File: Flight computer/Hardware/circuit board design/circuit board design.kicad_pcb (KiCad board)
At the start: 4 copper layers, 30.5 x 82.6 mm, 89 parts, among them J1 Conn_01x05, J2 USB_B_Micro, J3 Screw_Terminal_01x04, J4 Conn_01x02, J5 Screw_Terminal_01x04, J6 Conn_Coaxial, J7 Conn_Coaxial, U1 IIS2MDC, U10 BMI088, U11 ATSAML21J18B-AUT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

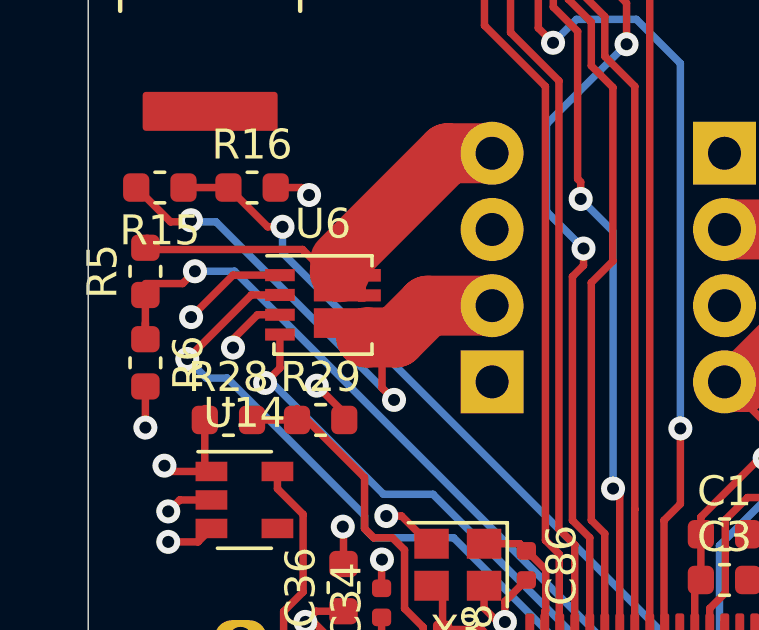
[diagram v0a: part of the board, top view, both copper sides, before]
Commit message: changed power plane to 3.3V, bringing v drive to pins via 2.54mm tracks
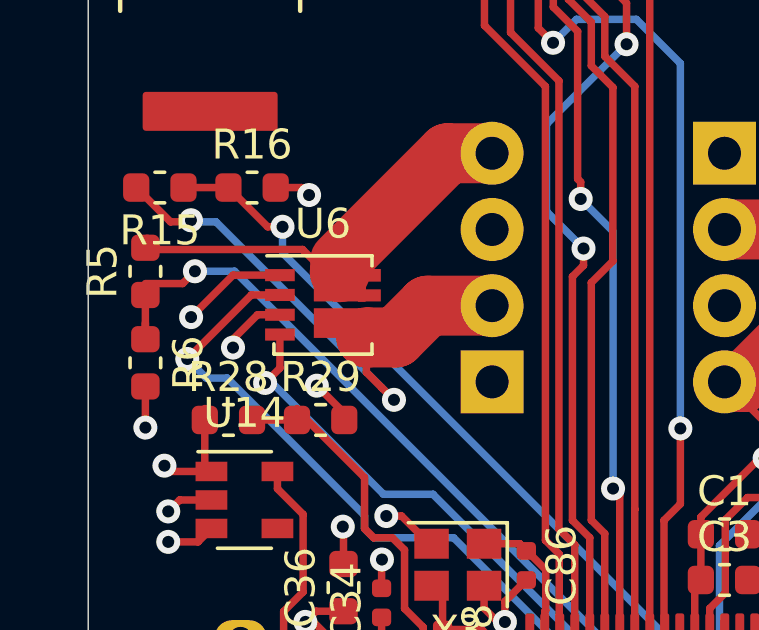
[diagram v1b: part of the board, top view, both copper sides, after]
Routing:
- net Vdrive: track 5.46 -> 67.1 mm
- added copper zone on VCC.Cu, net +3V3
- removed copper zone on VCC.Cu, net Vdrive
